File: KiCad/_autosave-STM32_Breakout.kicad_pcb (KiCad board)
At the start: 2 copper layers, 15.2 x 33 mm, 17 parts, among them J1 USB_B_Micro, J2 Conn_01x02, J3 Conn_01x12, J4 Conn_01x12, U1 STM32F042F6Px, U2 AP2127K-3.3

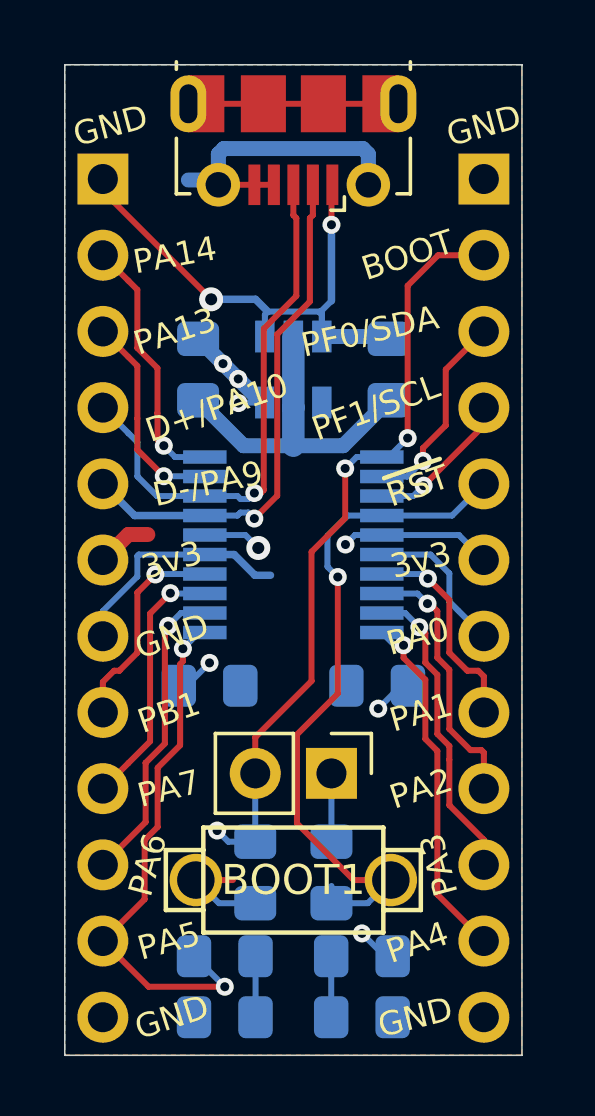
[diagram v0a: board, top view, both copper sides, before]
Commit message: Update for additional... something
Added silkscreen labels, moved SMD parts to bottom,
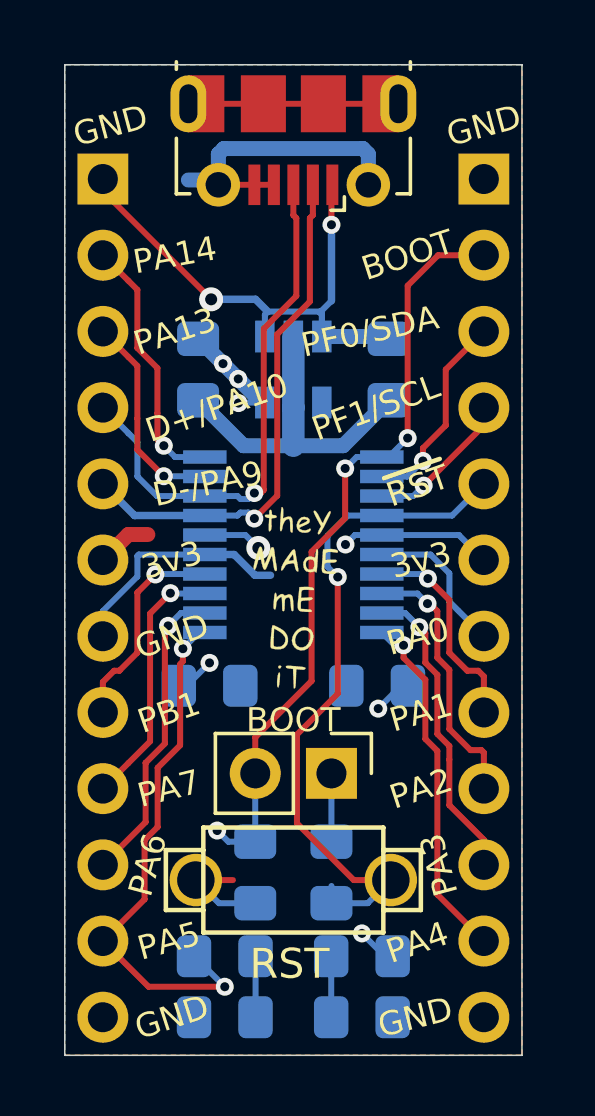
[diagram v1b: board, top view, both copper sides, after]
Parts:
- added G***: LOGO, TRA_KiCad_Footprints:VoronLogo_6pt5mm_silkScreen, B.Cu at (128.1, 76.1)
- added G***: LOGO, STM32_Breakout:THeyMadeME, F.Cu at (128.3, 90.2)
- renumbered BOOT1 to RST
